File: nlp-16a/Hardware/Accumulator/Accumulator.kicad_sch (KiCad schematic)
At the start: 46 parts, among them J1 Screw_Terminal_01x02, J2 Conn_02x10_Counter_Clockwise, J3 Conn_02x10_Counter_Clockwise, J4 Conn_02x10_Odd_Even, U17 CD74HC00

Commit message: アキュムレータ 更新
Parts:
- added C2, C22, C3, C4, C5, C6, C7, C8, C9: C, Capacitor_THT:C_Disc_D7.5mm_W2.5mm_P5.00mm, symbol Device:C
- added D18: LED, LED_THT:LED_D3.0mm, symbol Device:LED
- added J5: Conn_02x10_Odd_Even, Connector_PinHeader_2.54mm:PinHeader_2x10_P2.54mm_Horizontal, symbol Connector_Generic:Conn_02x10_Odd_Even
- added R18: R, Resistor_SMD:R_0603_1608Metric_Pad0.98x0.95mm_HandSolder, symbol Device:R
- J2, J3, J4: footprint Connector_PinHeader_2.54mm:PinHeader_2x10_P2.54mm_Vertical -> Connector_PinHeader_2.54mm:PinHeader_2x10_P2.54mm_Horizontal
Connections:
- net GND: now also C2.2, C22.2, C3.2, C4.2, C5.2, C6.2, C7.2, C8.2, C9.2, R18.2
- net VCC: now also C2.1, C22.1, C3.1, C4.1, C5.1, C6.1, C7.1, C8.1, C9.1
- net at U17.11: now also D18.2 (A)
- net Acc0/Q renamed DEBUG0
- net DEBUG0: now also J5.6 (Pin_6)
- net Acc1/Q renamed DEBUG1
- net DEBUG1: now also J5.8 (Pin_8)
- net Acc10/Q renamed DEBUG10
- net DEBUG10: now also J5.9 (Pin_9)
- net Acc11/Q renamed DEBUG11
- net DEBUG11: now also J5.11 (Pin_11)
- net Acc12/Q renamed DEBUG12
- net DEBUG12: now also J5.13 (Pin_13)
- net Acc13/Q renamed DEBUG13
- net DEBUG13: now also J5.15 (Pin_15)
- net Acc14/Q renamed DEBUG14
- net DEBUG14: now also J5.17 (Pin_17)
- net Acc15/Q renamed DEBUG15
- net DEBUG15: now also J5.19 (Pin_19)
- net Acc2/Q renamed DEBUG2
- net DEBUG2: now also J5.10 (Pin_10)
- net Acc3/Q renamed DEBUG3
- net DEBUG3: now also J5.12 (Pin_12)
- net Acc4/Q renamed DEBUG4
- net DEBUG4: now also J5.14 (Pin_14)
- net Acc5/Q renamed DEBUG5
- net DEBUG5: now also J5.16 (Pin_16)
- net Acc6/Q renamed DEBUG6
- net DEBUG6: now also J5.18 (Pin_18)
- net Acc7/Q renamed DEBUG7
- net DEBUG7: now also J5.20 (Pin_20)
- net Acc8/Q renamed DEBUG8
- net DEBUG8: now also J5.5 (Pin_5)
- net Acc9/Q renamed DEBUG9
- net DEBUG9: now also J5.7 (Pin_7)
- new net: D18.1 (K), R18.1
- no-connect marks 8 -> 11
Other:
- added sheet dmy_pad (dmy_pad.kicad_sch)
- moved on the sheet: H1, H2, H3, H4, J2, J3, J4

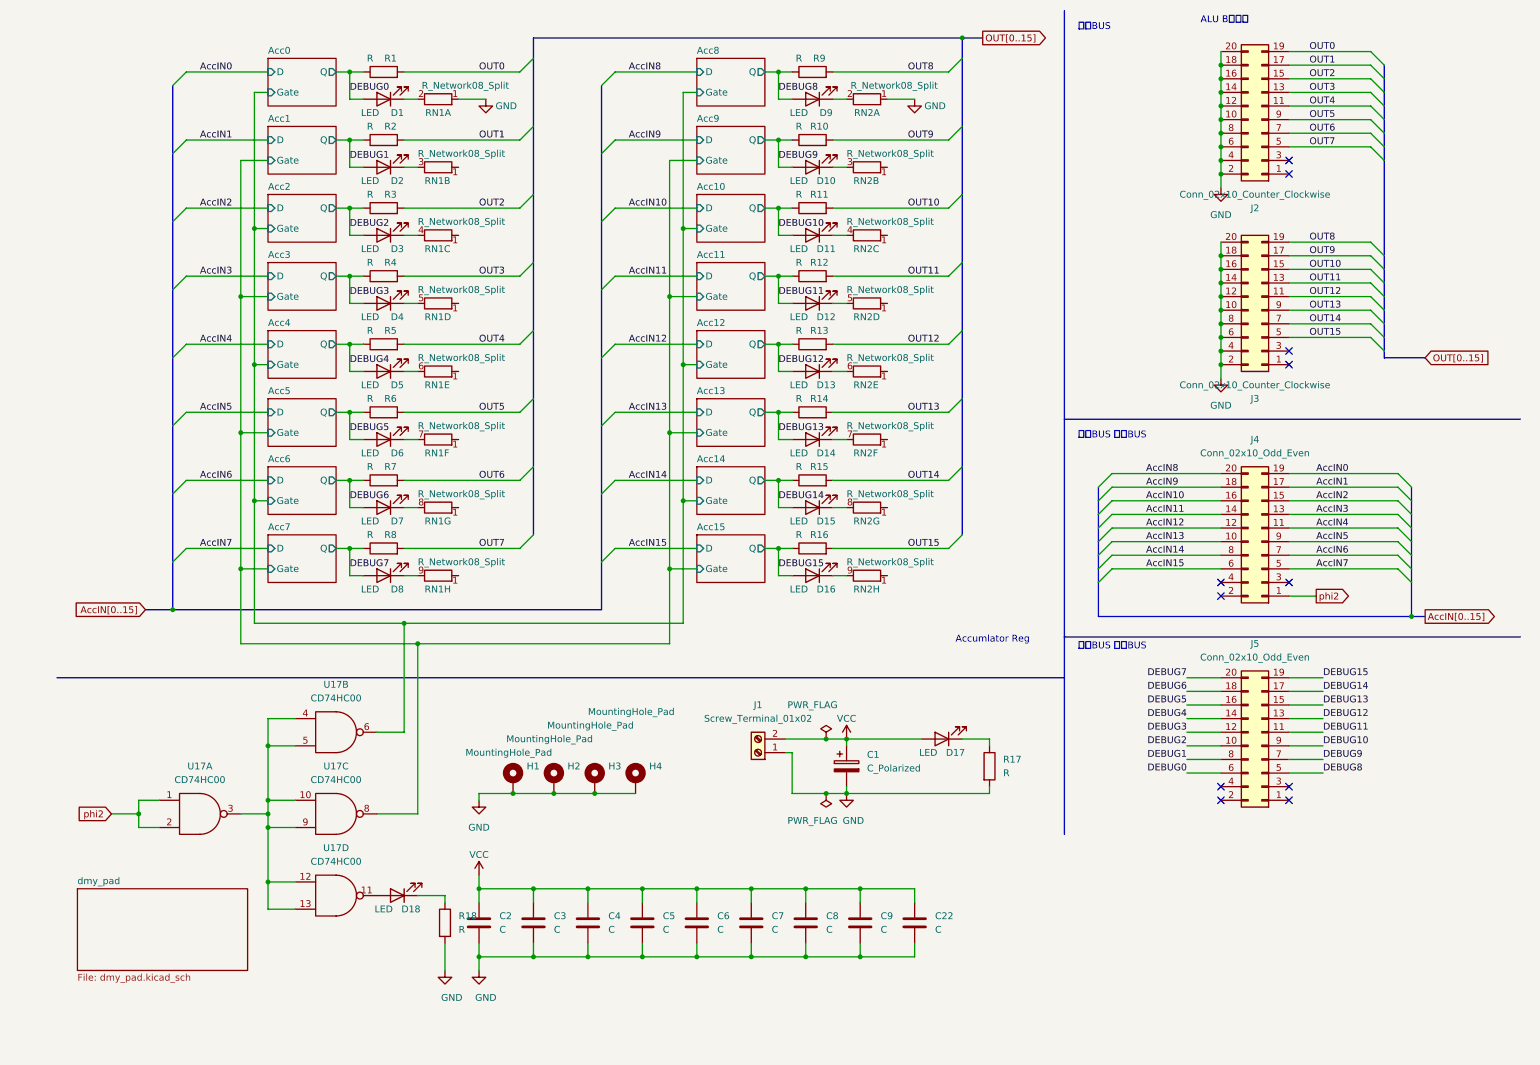
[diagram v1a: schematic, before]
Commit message: アキュムレータ書き込み条件変更(内部処理モードとAcc選択を追加)
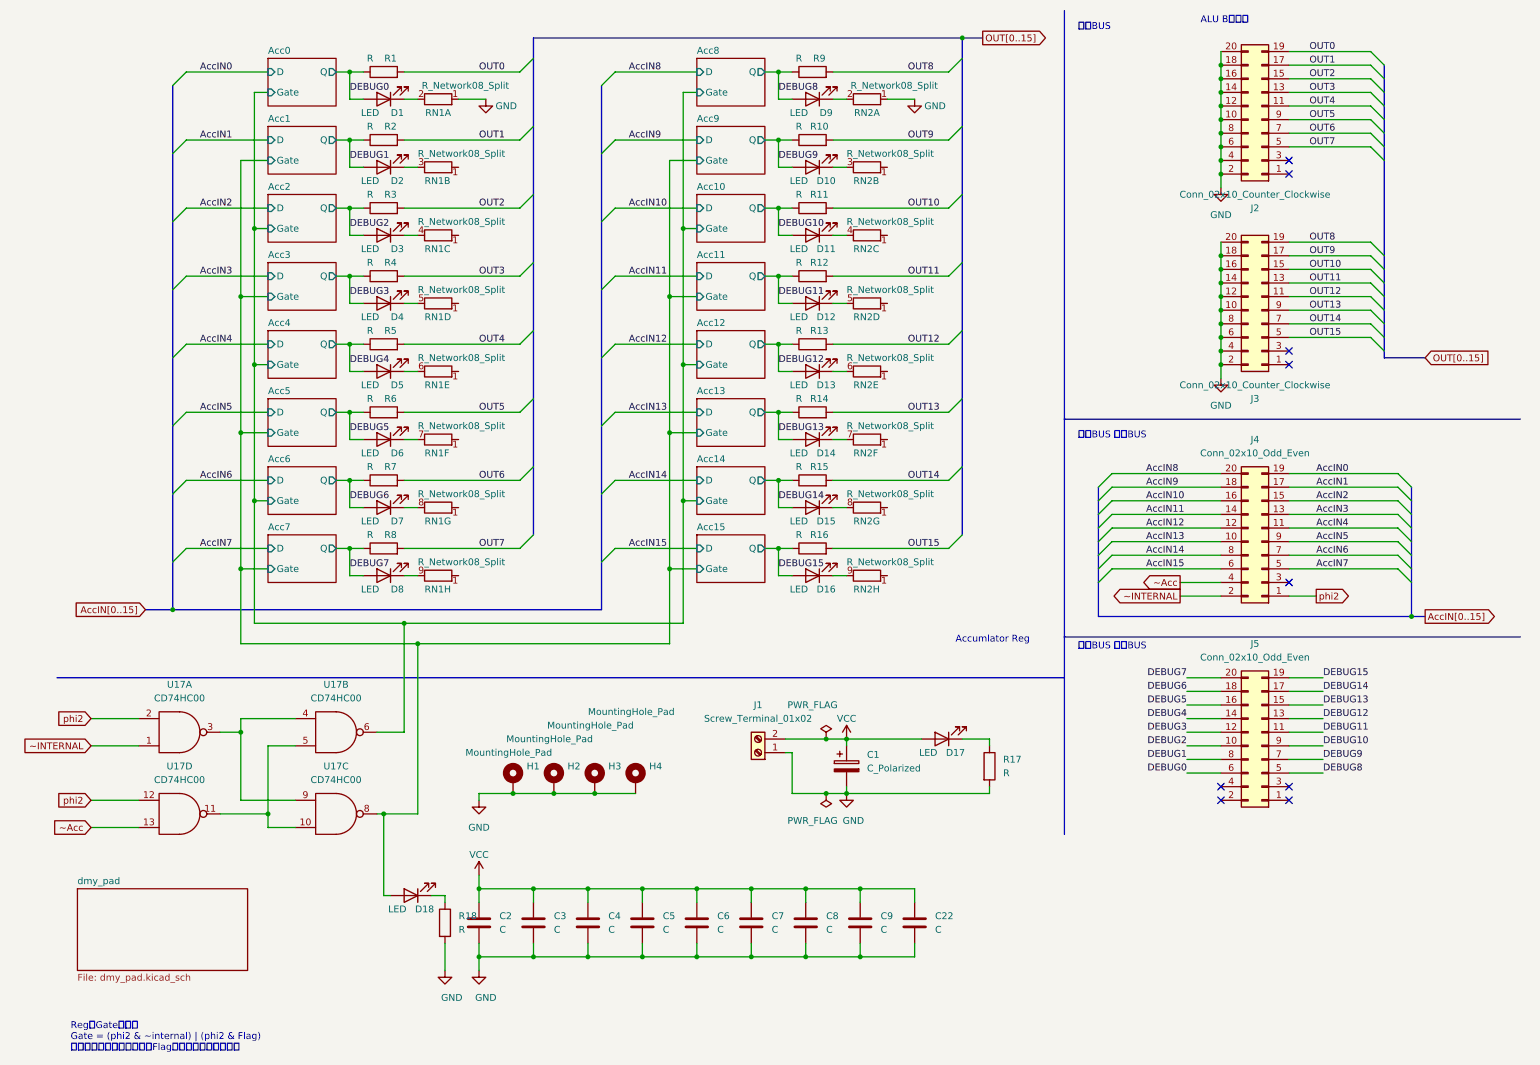
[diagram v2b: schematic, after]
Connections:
- net Acc1/Gate: now also D18.2 (A)
- net phi2: now also U17.12; no longer U17.1
- net at U17.11: now also U17.10, U17.5; no longer D18.2 (A)
- net ~INTERNAL: now reaches J4.2 (Pin_2)
- net ~INTERNAL: now also U17.1
- net ~Acc: now reaches J4.4 (Pin_4)
- net ~Acc: now also U17.13
- new net: U17.3, U17.4, U17.9
- no-connect marks 11 -> 9
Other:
- note added: "RegのGateを変更 Gate = (phi2 & ~internal) | (phi2 & Flag) 非内部処理モードもしくはFlagへ転送するときに更新"
- moved on the sheet: D18, U17A, U17D

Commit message: アキュムレータ修正
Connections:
- net Acc1/Gate: no longer D18.2 (A)
- net phi2: now also U17.1; no longer U17.12, U17.2
- net ~Acc: now also U17.2; no longer U17.13
- net ~INTERNAL: no longer U17.1
- net at U17.10, U17.5: now also U17.12, U17.13, U17.3, U17.4, U17.9; no longer U17.11
- new net: D18.2 (A), U17.11
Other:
- moved on the sheet: U17A, U17D

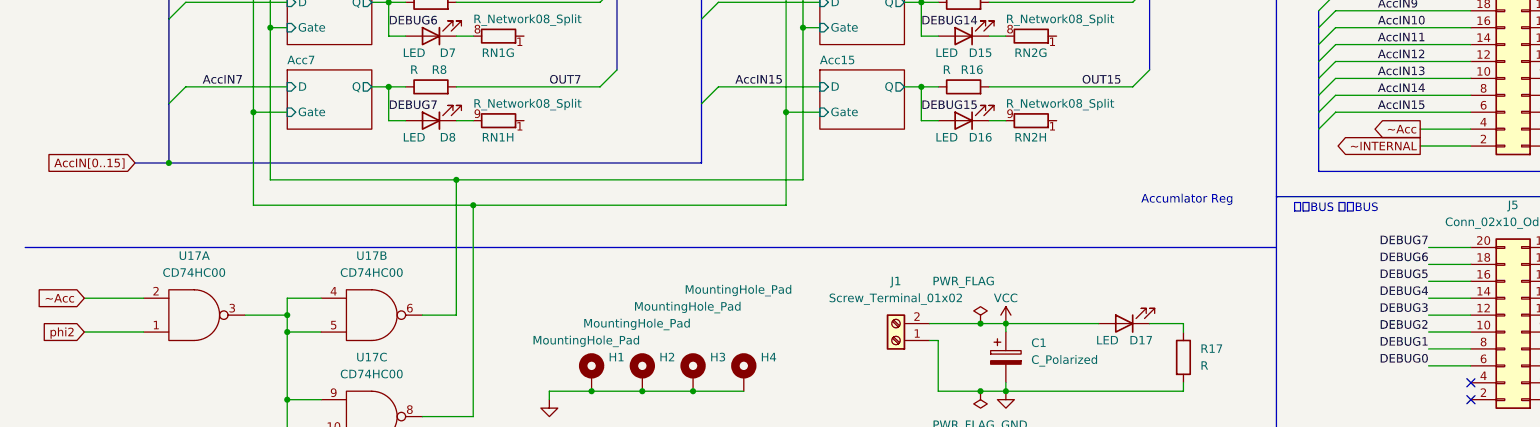
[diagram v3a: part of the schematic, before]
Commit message: v1.1全ガーバーを更新
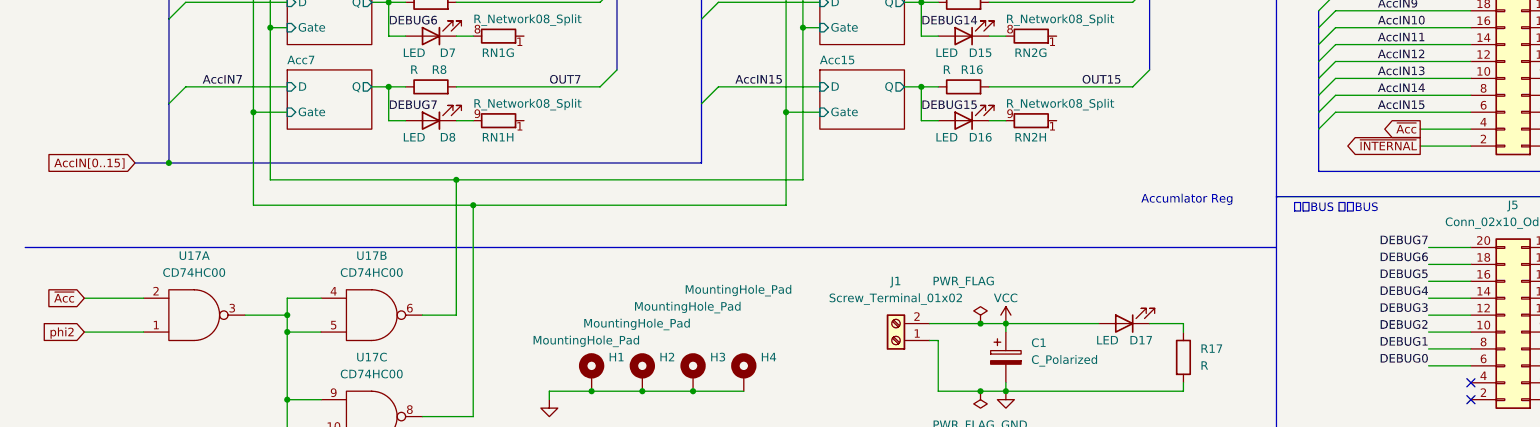
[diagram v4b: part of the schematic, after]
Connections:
- net ~Acc renamed ~{Acc}
- net ~INTERNAL renamed ~{INTERNAL}
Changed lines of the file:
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@@
     (effects (font (size 1.27 1.27)) (justify left bottom))
   )
-  (global_label "~Acc" (shape input) (at 20.32 144.78 180) (fields_autoplaced)
+  (global_label "~{Acc}" (shape input) (at 20.32 144.78 180) (fields_autoplaced)
     (effects (font (size 1.27 1.27)) (justify right))
-    (property "Intersheet References" "${INTERSHEET_REFS}" (id 0) (at 13.734 144.7006 0)
+    (property "Intersheet References" "${INTERSHEET_REFS}" (id 0) (at 14.6412 144.7006 0)
       (effects (font (size 1.27 1.27)) (justify right) hide)
     )
@@
     )
   )
-  (global_label "~Acc" (shape output) (at 220.98 119.38 180) (fields_autoplaced)
+  (global_label "~{Acc}" (shape output) (at 220.98 119.38 180) (fields_autoplaced)
     (effects (font (size 1.27 1.27)) (justify right))
-    (property "Intersheet References" "${INTERSHEET_REFS}" (id 0) (at 214.394 119.3006 0)
+    (property "Intersheet References" "${INTERSHEET_REFS}" (id 0) (at 215.3012 119.3006 0)
       (effects (font (size 1.27 1.27)) (justify right) hide)
     )
@@
     )
   )
-  (global_label "~INTERNAL" (shape output) (at 220.98 121.92 180) (fields_autoplaced)
+  (global_label "~{INTERNAL}" (shape output) (at 220.98 121.92 180) (fields_autoplaced)
     (effects (font (size 1.27 1.27)) (justify right))
-    (property "Intersheet References" "${INTERSHEET_REFS}" (id 0) (at 208.8907 121.8406 0)
+    (property "Intersheet References" "${INTERSHEET_REFS}" (id 0) (at 209.7979 121.8406 0)
       (effects (font (size 1.27 1.27)) (justify right) hide)
     )
